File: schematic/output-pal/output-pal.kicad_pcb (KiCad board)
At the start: 2 copper layers, 90 x 57 mm, 43 parts, among them SW1 SW_DIP_x02, U1 LM555xN, U4 AT28C64B-15PC, U5 HDSP-7503, U6 HDSP-7503, U7 HDSP-7503, U8 HDSP-7503, U9 GAL16V8

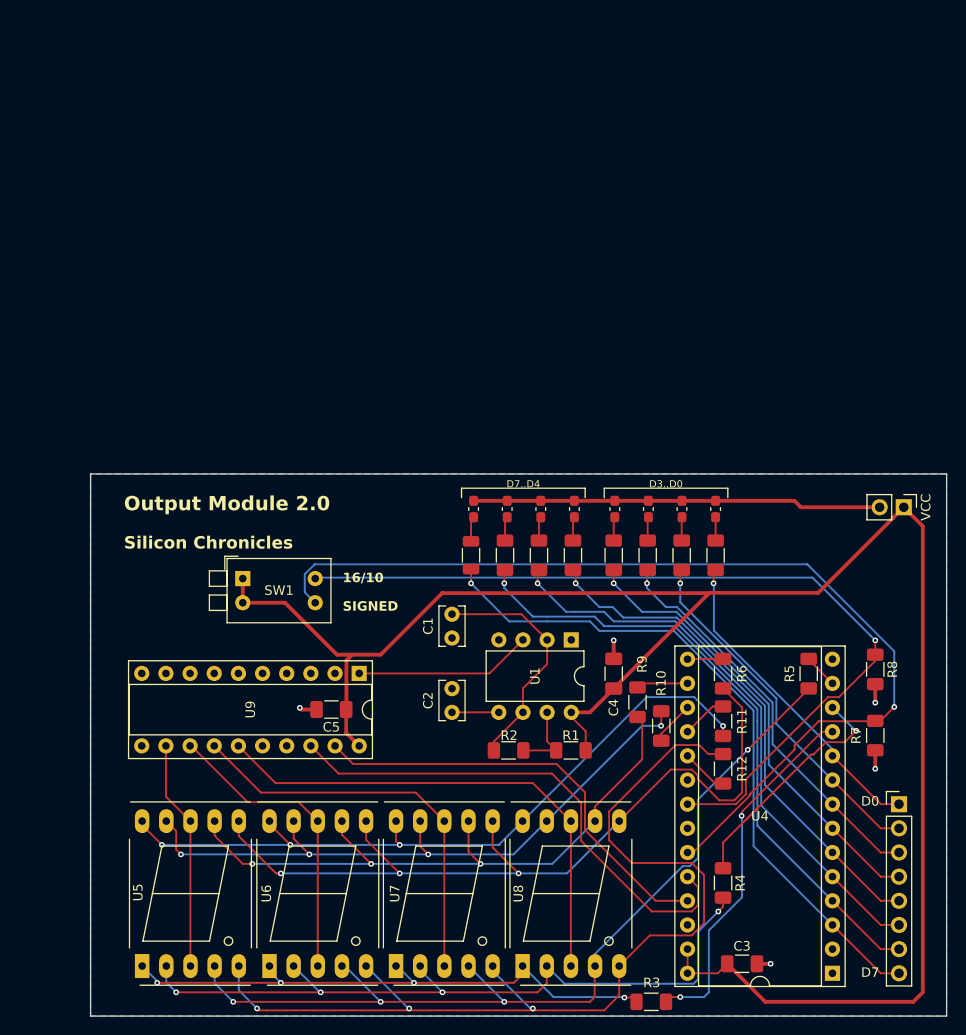
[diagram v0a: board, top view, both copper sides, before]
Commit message: New release of output.
Improved layout (more compact)
Bigger LEDs
More SMD components (including 7555 and capacitors)
Front copper fill
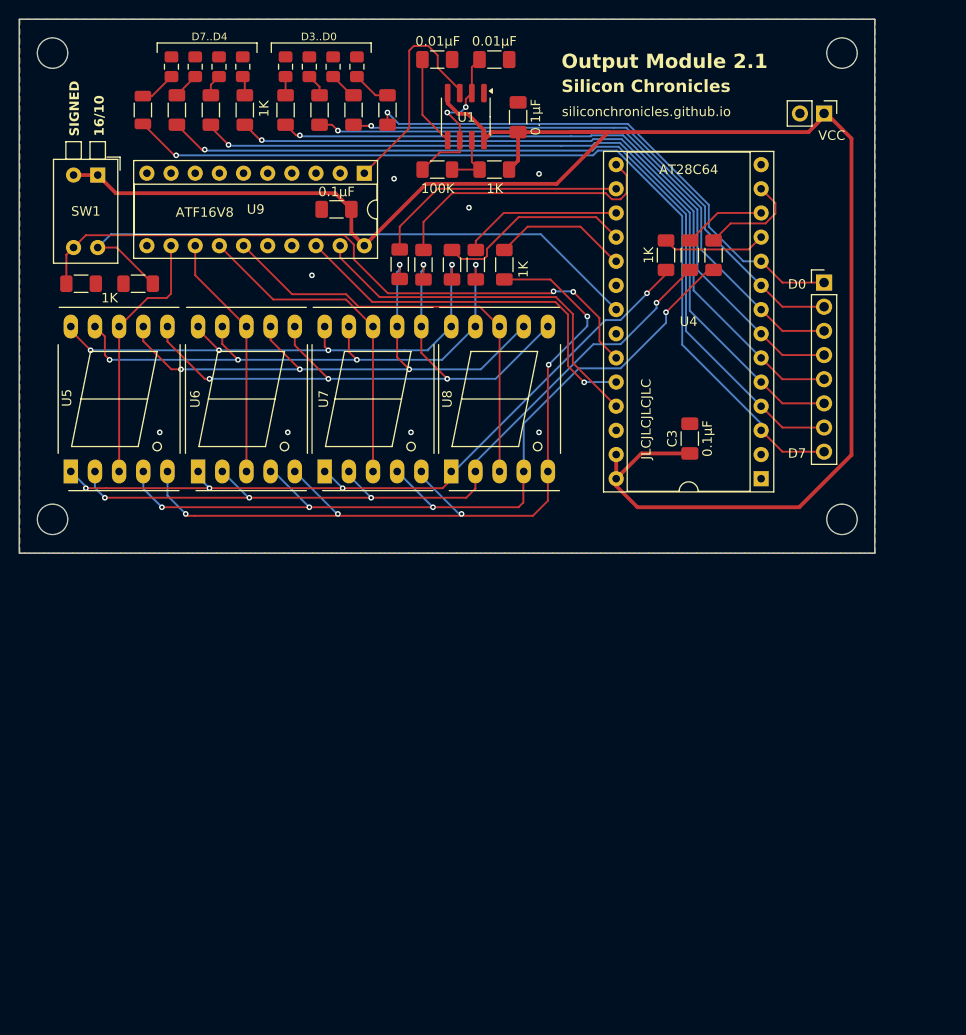
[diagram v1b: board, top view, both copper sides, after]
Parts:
- added REF**: MountingHole_3.2mm_M3, MountingHole:MountingHole_3.2mm_M3, F.Cu at (53.5, 80.8)
- added REF**: MountingHole_3.2mm_M3, MountingHole:MountingHole_3.2mm_M3, F.Cu at (136.5, 80.8)
- added REF**: MountingHole_3.2mm_M3, MountingHole:MountingHole_3.2mm_M3, F.Cu at (53.5, 31.8)
- added REF**: MountingHole_3.2mm_M3, MountingHole:MountingHole_3.2mm_M3, F.Cu at (136.5, 31.8)
- C1, C2: footprint Capacitor_THT:C_Rect_L4.0mm_W2.5mm_P2.50mm -> Capacitor_SMD:C_1206_3216Metric_Pad1.33x1.80mm_HandSolder
- D1, D2, D3, D4, D5, D6, D7, D8: footprint Capacitor_SMD:C_0603_1608Metric_Pad1.08x0.95mm_HandSolder -> Capacitor_SMD:C_0805_2012Metric_Pad1.18x1.45mm_HandSolder
- U1: value LM555xN -> 7555; footprint Package_DIP:DIP-8_W7.62mm -> Package_SO:SOIC-8_3.9x4.9mm_P1.27mm
- U4: value AT28C64B-15PC -> AT28C64
- U9: value GAL16V8 -> ATF16V8
- moved R7 96.1 mm to (56.5, 56.0), turned to 0 degrees
- moved R8 87.5 mm to (62.5, 56.0), turned to 180 degrees
- moved R3 78.5 mm to (118.0, 53.0), turned to -90 degrees
- moved C2 68.7 mm to (94.0, 32.4), turned to 0 degrees
- moved R4 66.1 mm to (120.5, 53.0)
- moved R1 61.6 mm to (100.0, 44.0)
- moved R2 61.5 mm to (94.0, 44.0)
- moved D1 59.9 mm to (85.5, 33.2)
- moved C4 59.4 mm to (102.5, 38.5)
- moved D2 59.2 mm to (83.0, 33.2)
- moved D3 58.6 mm to (80.5, 33.2)
- moved C1 58.5 mm to (100.0, 32.4), turned to 0 degrees
- moved R13 58.2 mm to (88.7, 37.7)
- moved R14 58.2 mm to (85.1, 37.7)
- moved R15 58.2 mm to (81.6, 37.7)
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- renumbered D0 to J1, VCC to J3
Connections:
- U1 pad 4: unconnected-(U1-R-Pad4) -> VCC
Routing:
- net GND: track 52.1 -> 0.00 mm, vias 5 -> 8
- net Net-(U4-A11): track 103.9 -> 69.5 mm, vias 1 -> 2
- net Net-(U4-I/O0): track 38.4 -> 10.9 mm, vias 2 -> 0
- net Net-(U4-I/O3): track 3.56 -> 29.9 mm
- net Net-(U4-A10): track 91.1 -> 65.7 mm, vias 1 -> 0
- net D5: track 60.4 -> 83.8 mm
- net D7: track 71.8 -> 95.2 mm
- net D4: track 54.2 -> 77.6 mm
- net D3: track 47.9 -> 71.0 mm
- net D6: track 66.3 -> 89.4 mm
- net D0: track 33.9 -> 56.8 mm
- net D2: track 42.5 -> 65.2 mm
- net Net-(U4-I/O4): track 4.83 -> 26.8 mm
- net /SEG.G: track 77.2 -> 56.5 mm
- net /SEG.B: track 87.9 -> 67.2 mm, vias 3 -> 4
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- added copper zone on F.Cu, net GND
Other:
- board size 90 x 57 mm -> 90 x 56.1 mm
- board text added: "JLCJLCJLCJLC"
- board text added: "Output Module 2.1"
- board text added: "VCC"
- board text added: "siliconchronicles.github.io"
- board text removed: "Output Module 2.0"
